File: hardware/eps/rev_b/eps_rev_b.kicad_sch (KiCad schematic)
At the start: 0 parts

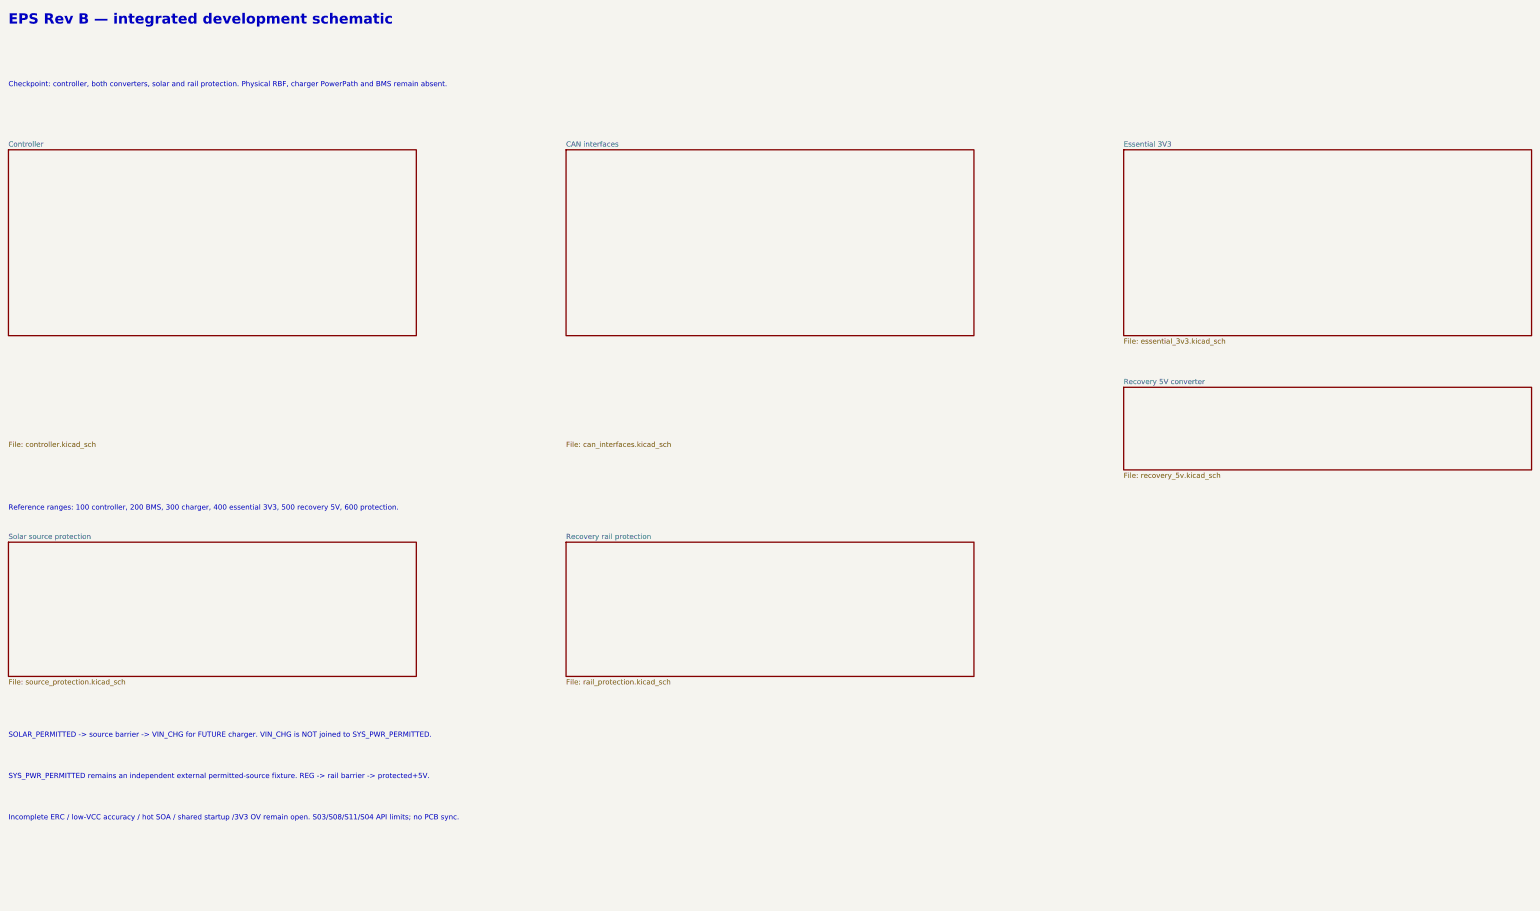
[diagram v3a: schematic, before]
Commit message: Integrate LTC4162 charger PowerPath and thermistor interface into EPS Rev B
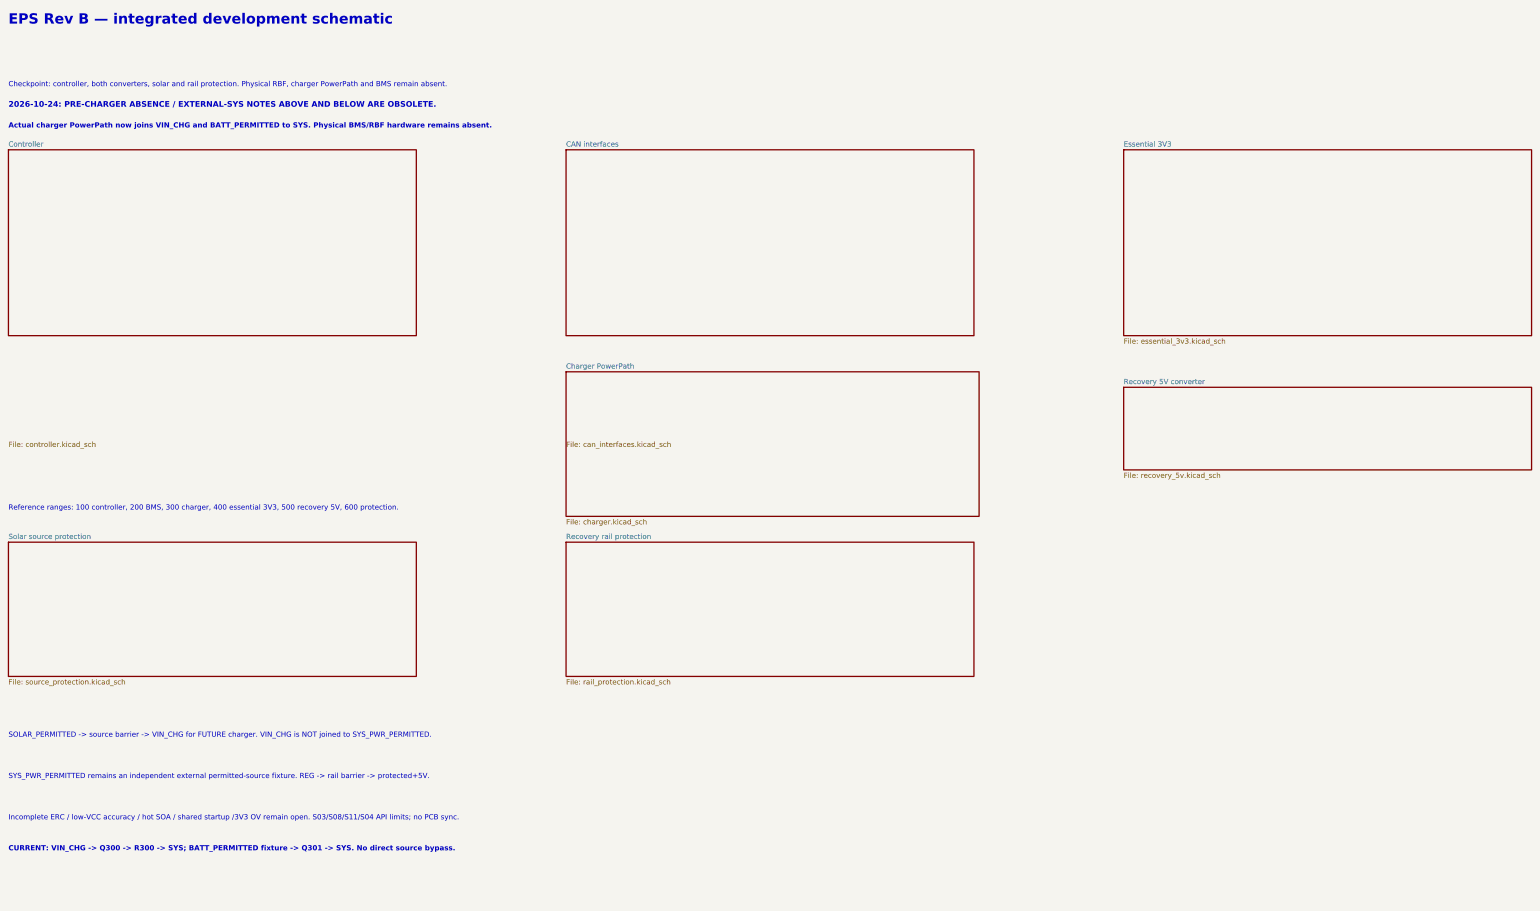
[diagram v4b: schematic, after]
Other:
- added sheet Charger PowerPath (charger.kicad_sch)
- note added: "2026-10-24: PRE-CHARGER ABSENCE / EXTERNAL-SYS NOTES ABOVE AND BELOW ARE OBSOLETE."
- note added: "Actual charger PowerPath now joins VIN_CHG and BATT_PERMITTED to SYS. Physical BMS/RBF hardware remains absent."
- note added: "CURRENT: VIN_CHG -> Q300 -> R300 -> SYS; BATT_PERMITTED fixture -> Q301 -> SYS. No direct source bypass."
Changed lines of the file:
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@@
     (effects (font (size 1.27 1.27)) (justify left bottom))
   )
+	(sheet
+		(at 167.64 115.57)
+		(size 101.6 35.56)
+		(fields_autoplaced)
+		(stroke
+			(width 0.1524)
+			(type solid)
+		)
+		(fill
+			(color 0 0 0 0.0)
+		)
+		(property "Sheetname" "Charger PowerPath"
+			(at 167.64 114.935 0)
+			(effects
+				(font
+					(size 1.27 1.27)
+				)
+				(justify left bottom)
+			)
+		)
+		(property "Sheetfile" "charger.kicad_sch"
+			(at 167.64 151.765 0)
+			(effects
+				(font
+					(size 1.27 1.27)
+				)
+				(justify left top)
+			)
+		)
+		(instances
+			(project "eps_rev_b"
+				(path "/8eba9f22-6f11-42d7-8e4a-b8de8905b113"
+					(page "8")
+				)
+			)
+		)
+	)
+  (text "2026-10-24: PRE-CHARGER ABSENCE / EXTERNAL-SYS NOTES ABOVE AND BELOW ARE OBSOLETE."
+    (at 30.48 50.8 0)
+    (effects (font (size 1.4 1.4) (bold yes)) (justify left bottom))
+  )
+  (text "Actual charger PowerPath now joins VIN_CHG and BATT_PERMITTED to SYS. Physical BMS/RBF hardware remains absent."
+    (at 30.48 55.88 0)
+    (effects (font (size 1.27 1.27) (bold yes)) (justify left bottom))
+  )
+  (text "CURRENT: VIN_CHG -> Q300 -> R300 -> SYS; BATT_PERMITTED fixture -> Q301 -> SYS. No direct source bypass."
+    (at 30.48 233.68 0)
+    (effects (font (size 1.27 1.27) (bold yes)) (justify left bottom))
+  )
 )

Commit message: Integrate EPS Rev B battery management development circuit
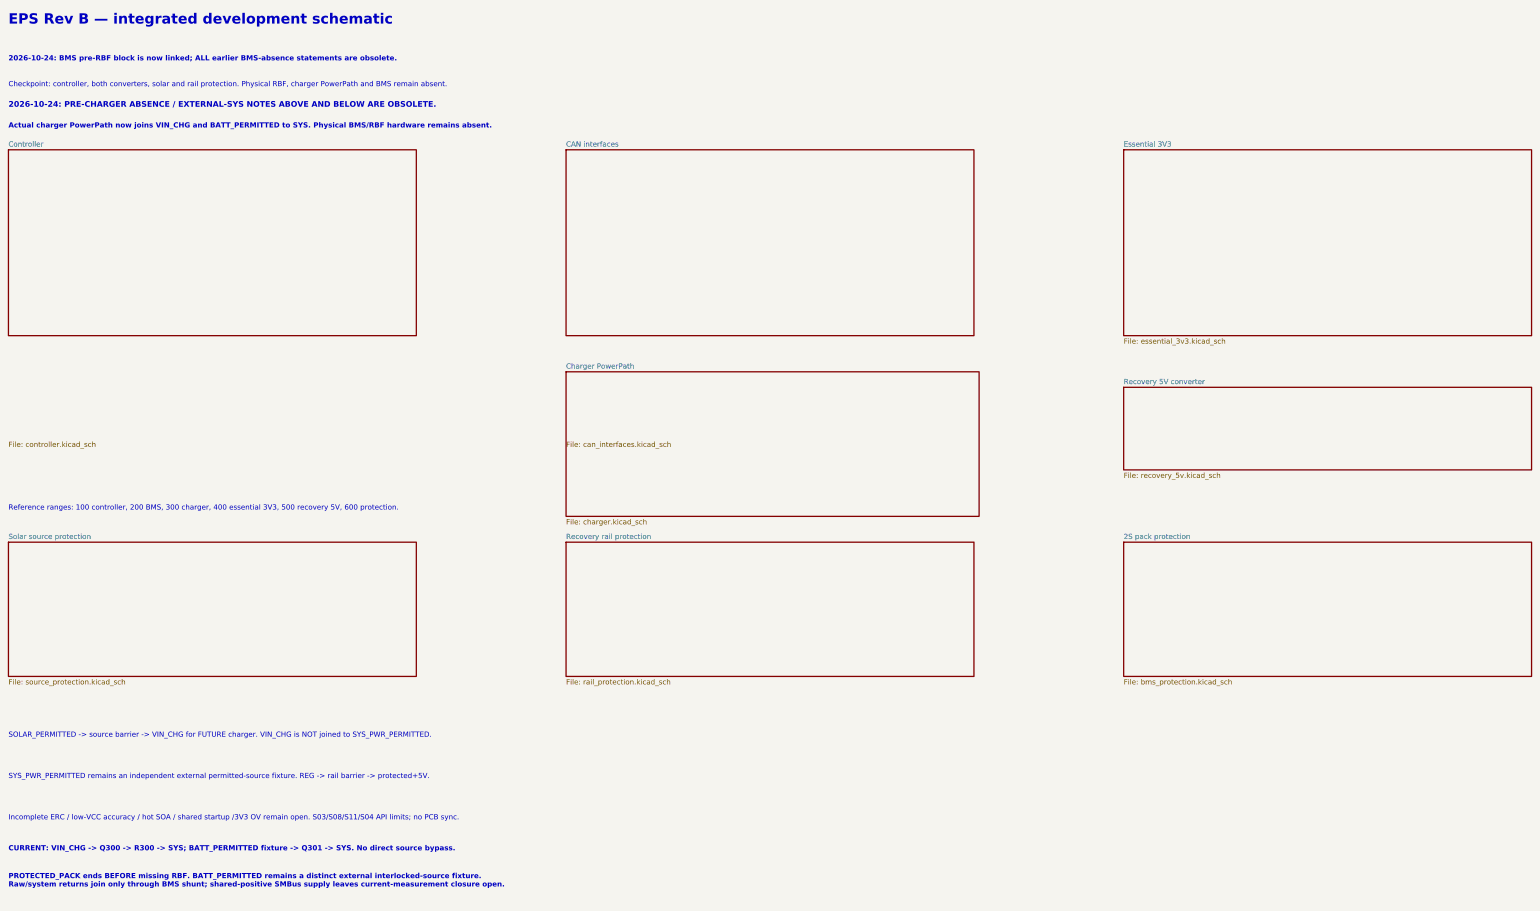
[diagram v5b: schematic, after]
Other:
- added sheet 2S pack protection (bms_protection.kicad_sch)
- note added: "2026-10-24: BMS pre-RBF block is now linked; ALL earlier BMS-absence statements are obsolete."
- note added: "PROTECTED_PACK ends BEFORE missing RBF. BATT_PERMITTED remains a distinct external interlocked-source fixture. Raw/system returns join only through BMS shunt; shared-positive SMBus supply leaves current-measurement closure open."
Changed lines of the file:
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@@
+    (effects (font (size 1.27 1.27) (bold yes)) (justify left bottom))
+  )
+	(sheet
+    (at 304.8 157.48)
+    (size 100.33 33.02)
+    (fields_autoplaced yes)
+    (stroke (width 0.1524) (type solid))
+    (fill (color 0 0 0 0.0))
+    (property "Sheetname" "2S pack protection"
+      (at 304.8 156.845 0)
+      (effects (font (size 1.27 1.27)) (justify left bottom))
+    )
+    (property "Sheetfile" "bms_protection.kicad_sch"
+      (at 304.8 191.135 0)
+      (effects (font (size 1.27 1.27)) (justify left top))
+    )
+    (instances
+      (project "eps_rev_b"
+        (path "/8eba9f22-6f11-42d7-8e4a-b8de8905b113" (page "9"))
+      )
+    )
+  )
+  (text "2026-10-24: BMS pre-RBF block is now linked; ALL earlier BMS-absence statements are obsolete."
+    (at 30.48 39.37 0)
+    (effects (font (size 1.27 1.27) (bold yes)) (justify left bottom))
+  )
+  (text "PROTECTED_PACK ends BEFORE missing RBF. BATT_PERMITTED remains a distinct external interlocked-source fixture.\nRaw/system returns join only through BMS shunt; shared-positive SMBus supply leaves current-measurement closure open."
+    (at 30.48 242.57 0)
     (effects (font (size 1.27 1.27) (bold yes)) (justify left bottom))
   )

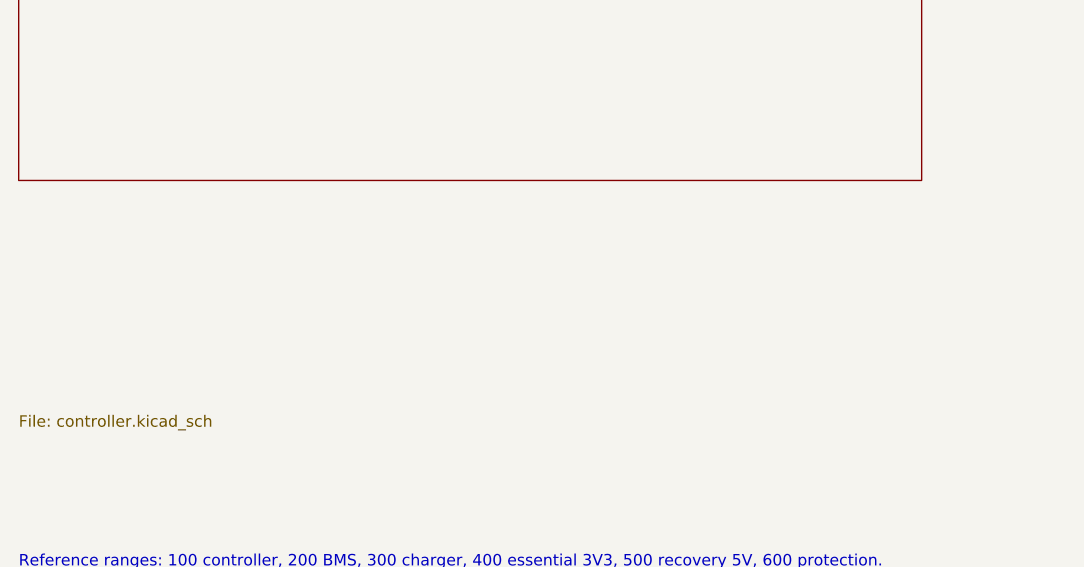
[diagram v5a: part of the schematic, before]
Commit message: Integrate buffered EPS UART debug interface
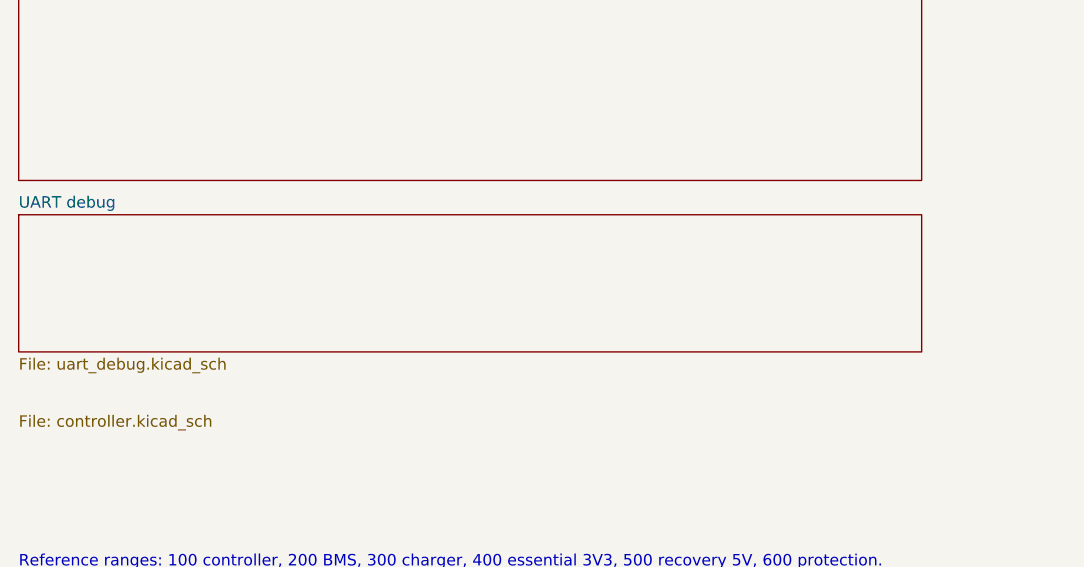
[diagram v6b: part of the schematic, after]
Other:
- added sheet UART debug (uart_debug.kicad_sch)
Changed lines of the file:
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@@
     (effects (font (size 1.27 1.27) (bold yes)) (justify left bottom))
   )
+	(sheet
+    (at 30.48 110.49)
+    (size 100.33 15.24)
+    (fields_autoplaced yes)
+    (stroke (width 0.1524) (type solid))
+    (fill (color 0 0 0 0.0))
+    (property "Sheetname" "UART debug"
+      (at 30.48 109.85499999999999 0)
+      (effects (font (size 1.27 1.27)) (justify left bottom))
+    )
+    (property "Sheetfile" "uart_debug.kicad_sch"
+      (at 30.48 126.365 0)
+      (effects (font (size 1.27 1.27)) (justify left top))
+    )
+    (instances
+      (project "eps_rev_b"
+        (path "/8eba9f22-6f11-42d7-8e4a-b8de8905b113" (page "10"))
+      )
+    )
+  )
 )
